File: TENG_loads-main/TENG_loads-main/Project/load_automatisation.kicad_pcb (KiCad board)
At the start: 2 copper layers, 263.4 x 251.4 mm, 125 parts, among them IC1 OPA2145IDR, IC10 TBD62083AFG, IC11 74HC238D,653, IC2 TBD62083AFG, IC3 TBD62083AFG, IC4 74HC238D,653, IC5 74HC238D,653, IC6 TBD62083AFG, IC7 TBD62083AFG, IC8 TBD62083AFG, IC9 OPA145IDBVT, J1 PowerNeg, J12 PH-2X05SG, J13 1757242, J2 1757242, J3 1757242, J30 1757349, J4 PowerIn, K1 V23079A1001B301, K10 IMC03TS, K11 V23079A1001B301, K12 V23079A1001B301, K13 V23079A1001B301, K14 IMC03TS, K15 IMC03TS, K16 IMC03TS, K17 V23079A1001B301, K18 V23079A1001B301, K19 V23079A1001B301, K2 V23079A1001B301, K20 V23079A1001B301, K21 V23079A1001B301, K22 IMC03TS, K23 IMC03TS, K24 IMC03TS, K25 IMC03TS, K26 IMC03TS, K27 V23079A1001B301, K28 V23079A1001B301, K29 V23079A1001B301, K3 V23079A1001B301, K30 IMC03TS, K31 IMC03TS, K32 IMC03TS, K33 V23079A1001B301, K34 V23079A1001B301, K35 V23079A1001B301, K36 V23079A1001B301, K37 V23079A1001B301, K38 IMC03TS, K39 IMC03TS, K4 V23079A1001B301, K40 IMC03TS, K41 IMC03TS, K42 IMC03TS, K43 V23079A1001B301, K44 V23079A1001B301, K45 V23079A1001B301, K46 IMC03TS, K47 IMC03TS, K48 IMC03TS, K5 V23079A1001B301, K6 IMC03TS, K7 IMC03TS, K8 IMC03TS, K9 IMC03TS, U1 AMS1117-5.0, U2 INA128, U3 AMS1117-5.0

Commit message: Pull Down Resistor and reconnect
Introduced the pull down resistors and reconnect all the unconnected tracks. The position of some items has changed to fit the new components.
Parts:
- added R10: 100k, Resistor_SMD:R_0805_2012Metric, F.Cu at (272.1, 242.7)
- added R11: 100k, Resistor_SMD:R_0805_2012Metric, F.Cu at (227.2, 244.6)
- added R12: 100k, Resistor_SMD:R_0805_2012Metric, F.Cu at (224.8, 244.6)
- added R7: 100k, Resistor_SMD:R_0805_2012Metric, F.Cu at (243.8, 184.1)
- added R8: 100k, Resistor_SMD:R_0805_2012Metric, F.Cu at (248.8, 184.1)
- added R9: 100k, Resistor_SMD:R_0805_2012Metric, F.Cu at (272.1, 240.6)
- moved J3 37.5 mm to (128.7, 153.7)
- moved J2 37.3 mm to (128.7, 169.0)
- moved J1 27.2 mm to (136.7, 156.2), turned to 0 degrees
- moved J4 24.9 mm to (136.4, 171.5), turned to 0 degrees
- moved C1 10.0 mm to (146.4, 172.8)
- moved C15 10.0 mm to (146.7, 155.0)
- moved C16 10.0 mm to (167.8, 155.6)
- moved C17 10.0 mm to (207.2, 158.9)
- moved C18 10.0 mm to (202.3, 178.8)
- moved C2 10.0 mm to (167.8, 173.4)
- moved C20 10.0 mm to (202.0, 163.5)
- moved C3 10.0 mm to (208.8, 172.7)
- moved C4 10.0 mm to (202.6, 156.6)
- moved IC9 10.0 mm to (202.4, 160.2)
- moved J12 10.0 mm to (180.8, 153.4)
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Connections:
- IC11 pad 4: /Din3 -> Net-(IC11-~{E1})
- IC11 pad 5: /Din4 -> Net-(IC11-~{E2})
- IC4 pad 4: /Din3 -> Net-(IC4-~{E1})
- IC4 pad 5: /Din5 -> Net-(IC4-~{E2})
- IC5 pad 4: /Din4 -> Net-(IC5-~{E1})
- IC5 pad 5: /Din5 -> Net-(IC5-~{E2})
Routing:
- net /TengN_sw: track 35.6 -> 715.4 mm, vias 0 -> 1
- net /Teng-: track 839.0 -> 217.7 mm, vias 1 -> 0
- net /Din3: track 233.2 -> 117.2 mm, vias 3 -> 2
- net /Din5: track 255.3 -> 163.1 mm, vias 2 -> 0
- net /Din4: track 232.6 -> 164.9 mm, vias 4 -> 2
- net VCC: track 351.7 -> 304.5 mm, vias 5 -> 4
- net GND: track 793.2 -> 762.8 mm, vias 18 -> 19
- net Net-(IC11-~{E1}): track 0.00 -> 17.9 mm
- net Net-(IC11-~{E2}): track 0.00 -> 13.6 mm
- net /Dout2: track 76.6 -> 87.5 mm
- net /TengN_IN: track 47.1 -> 57.6 mm
- net Net-(J1-Pin_2): track 0.00 -> 7.98 mm
- net Net-(J4-Pin_2): track 0.00 -> 7.67 mm
- net Net-(IC4-~{E2}): track 0.00 -> 6.40 mm
- net -VCC: track 185.0 -> 178.7 mm
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
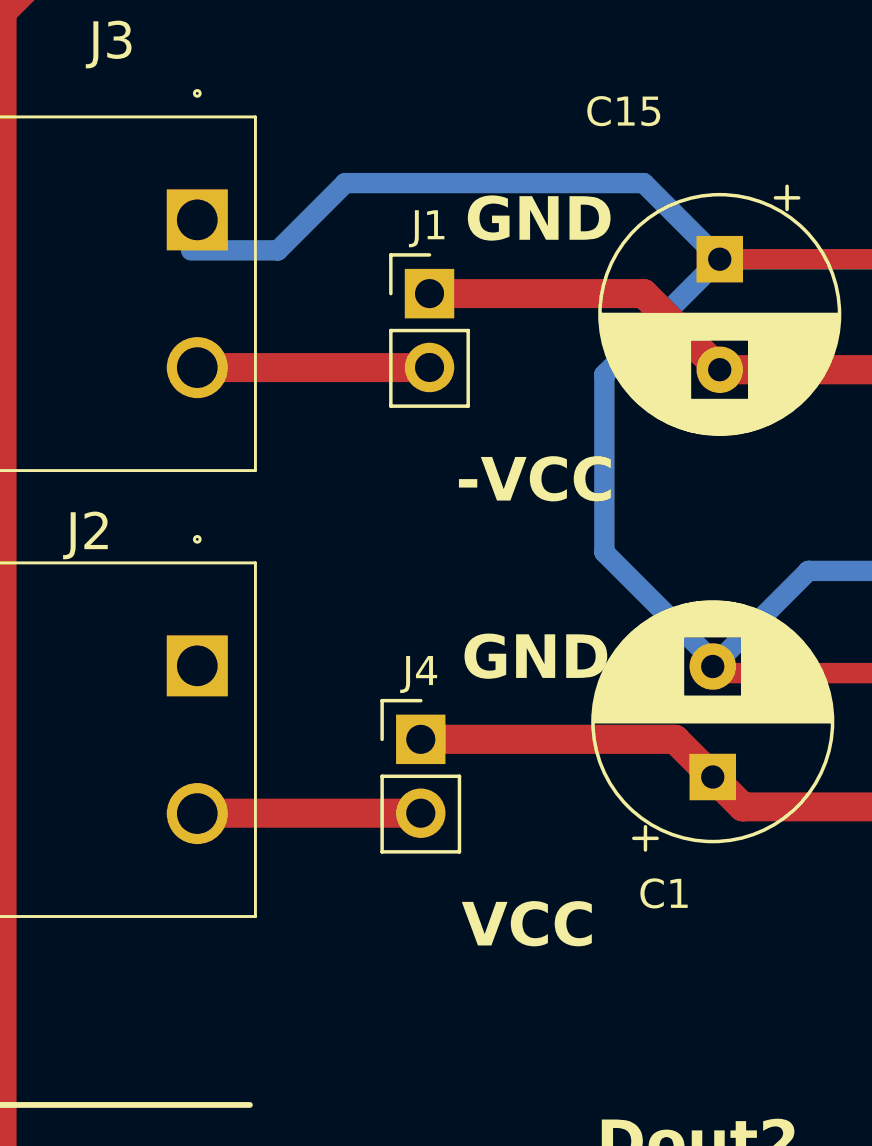
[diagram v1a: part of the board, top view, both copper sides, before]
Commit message: Little adjustments
Little adjustments: Position correction in jumper
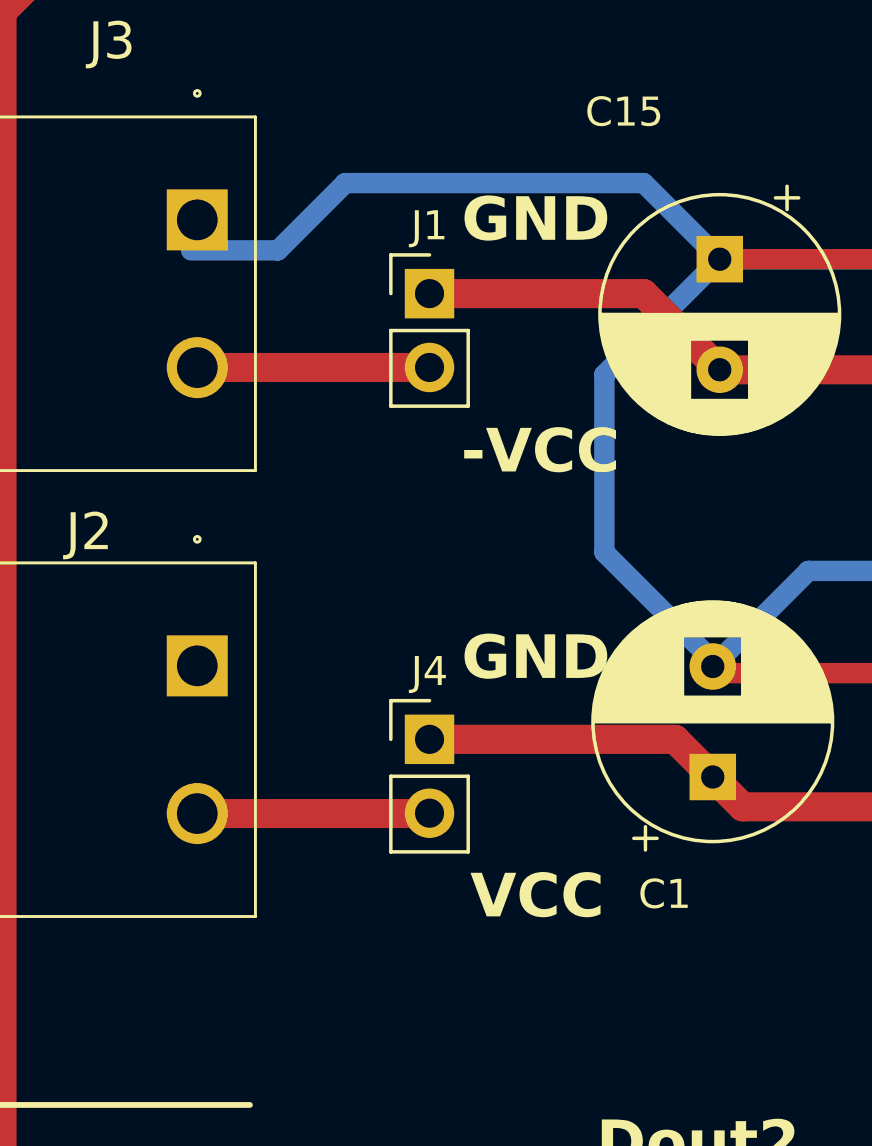
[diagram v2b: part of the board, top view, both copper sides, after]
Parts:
- moved J4 0.30 mm to (136.7, 171.5)

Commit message: Fix TENg buffer, ans some placements
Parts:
- moved R7 20.7 mm to (260.4, 196.5), turned to 0 degrees
- moved R8 15.9 mm to (261.7, 193.5), turned to 0 degrees
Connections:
- IC1 pad 5: /Teng- -> /TengN_sw
- J12 pad 10: /Current_Sense2_OUT -> /Current_Sense2_IN
- J12 pad 6: /Current_Sense2_IN -> /Current_Sense2_OUT
- J12 pad 8: /Current_Sense2_OUT -> /Current_Sense2_IN
- J30 pad 9: unconnected-(J30-Pad9) -> GND
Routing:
- net /Teng-: track 217.7 -> 37.0 mm
- net /TengN_sw: track 715.4 -> 790.6 mm, vias 1 -> 2
- net Net-(IC11-~{E1}): track 17.9 -> 10.2 mm
- net GND: track 762.8 -> 769.9 mm, vias 19 -> 20
- net Net-(IC11-~{E2}): track 13.6 -> 7.19 mm
- net /Din5: track 163.1 -> 166.9 mm
- net /TengN_IN: track 57.6 -> 59.8 mm
- net /Current_Sense2_OUT: track 25.1 -> 26.2 mm, vias 1 -> 0

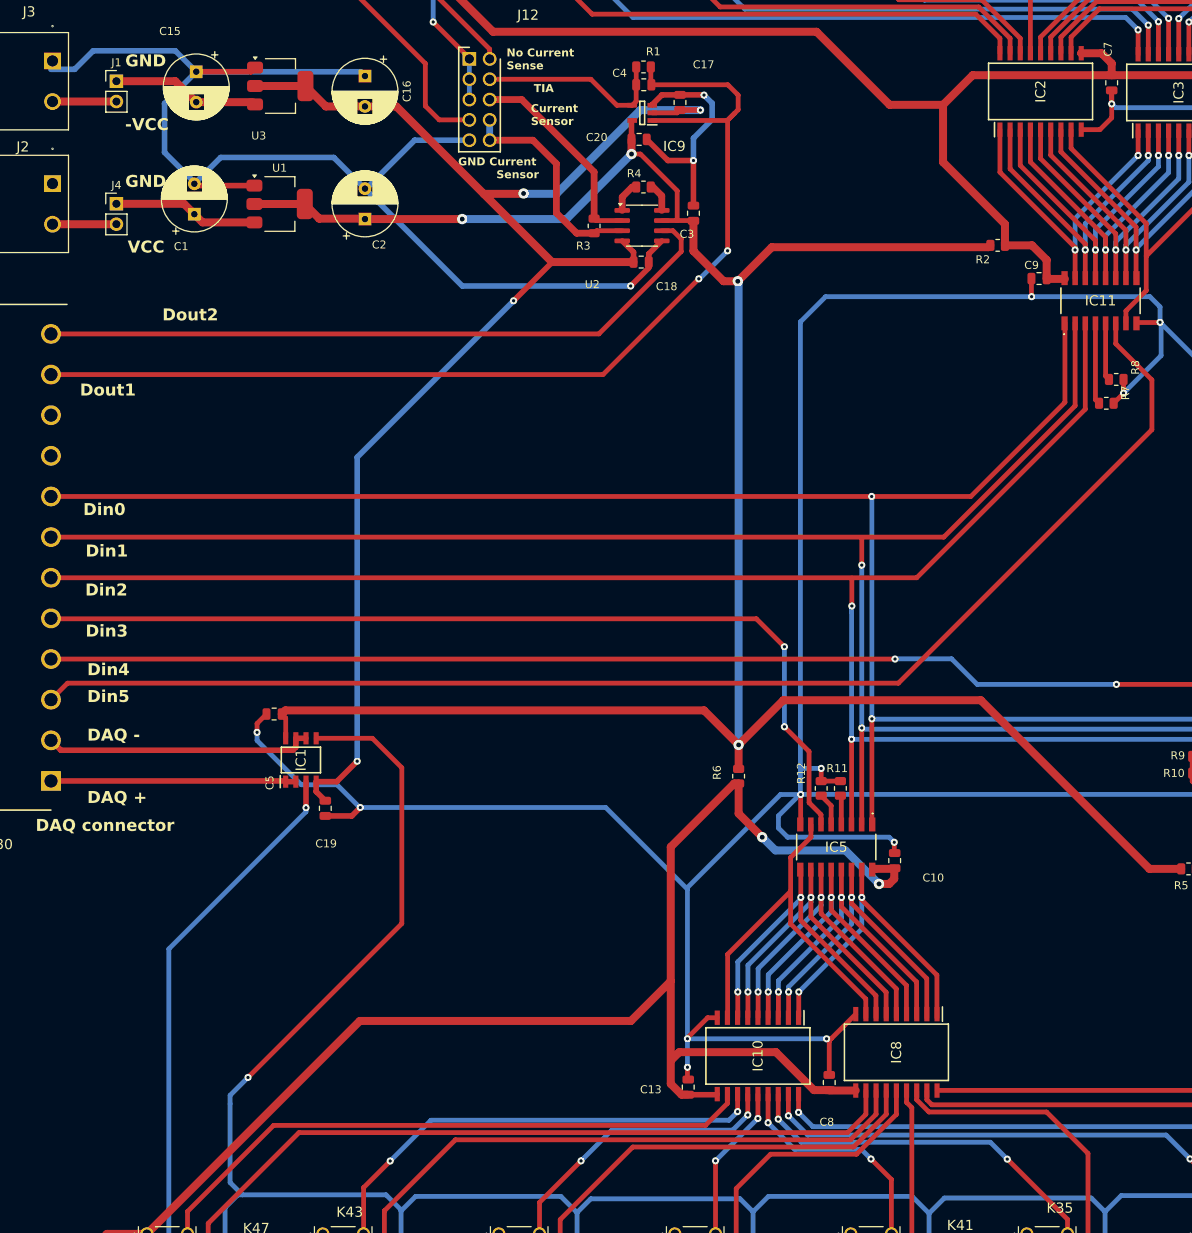
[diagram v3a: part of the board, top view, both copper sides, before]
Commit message: Fix ground pin, change sheet name, move 2 silkscreen labels
1) Sheet name : Root

2) Changed the position of 2 silkscreen labels

3) Connect unconnected ground
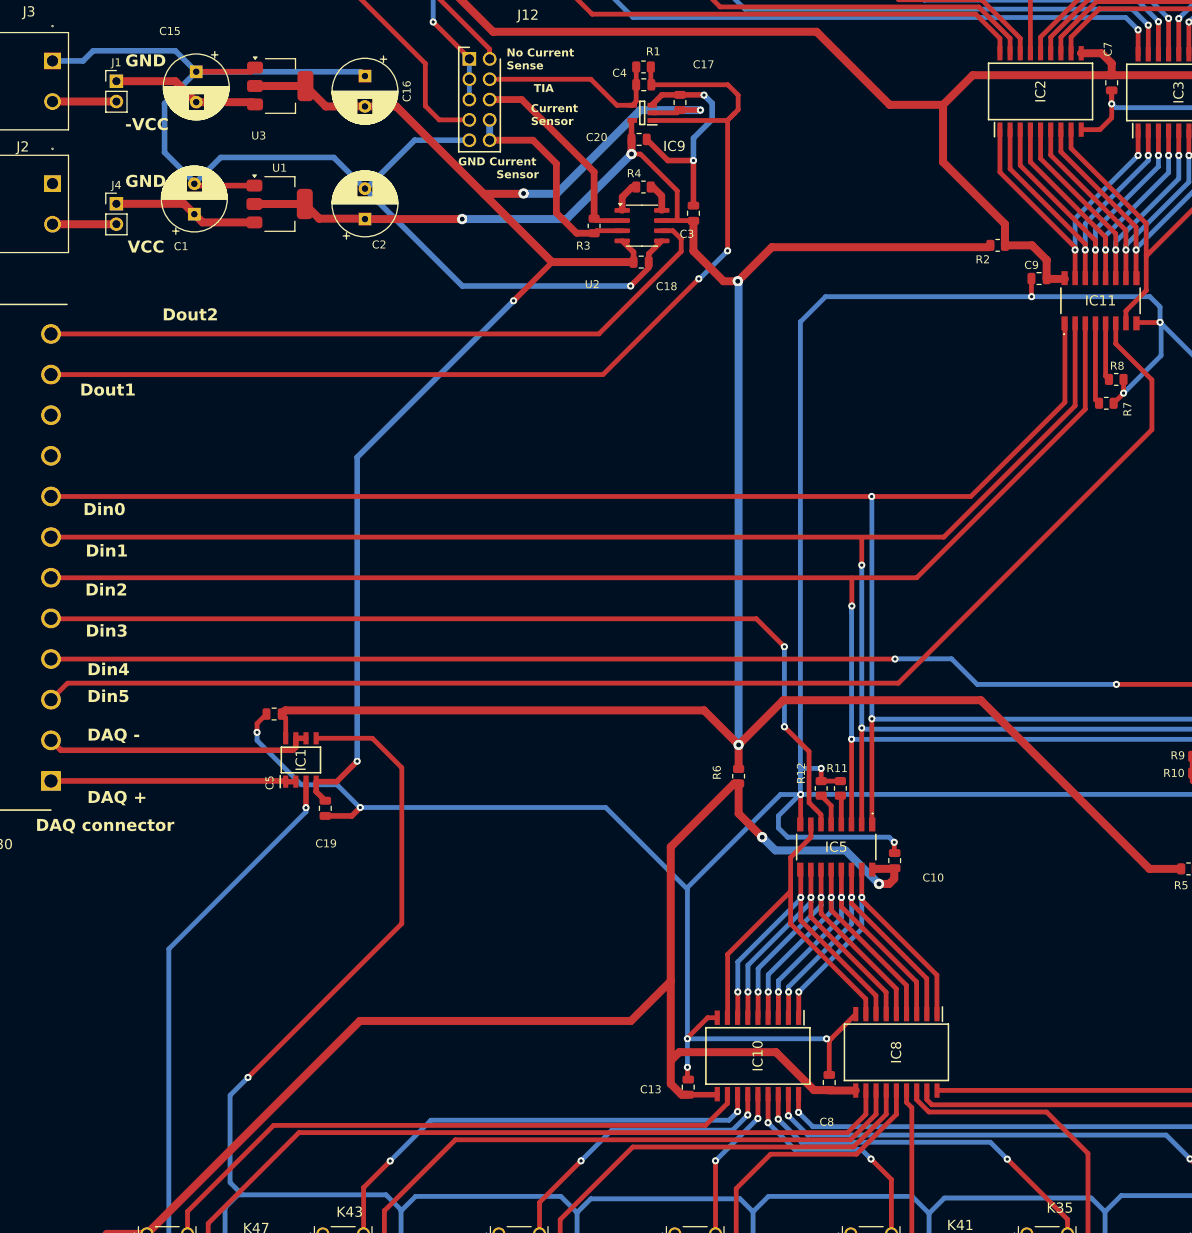
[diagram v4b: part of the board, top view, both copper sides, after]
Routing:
- net GND: track 769.9 -> 769.3 mm
